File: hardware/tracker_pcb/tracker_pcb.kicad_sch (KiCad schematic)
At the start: 36 parts, among them IC1 DRV8244HQRYJRQ1, IC2 DRV8244HQRYJRQ1, IC3 THVD1426DRLR, J1 256-406, U1 TPS62933FDRLR, U2 ESP32C6_SEEED, X1 256-402

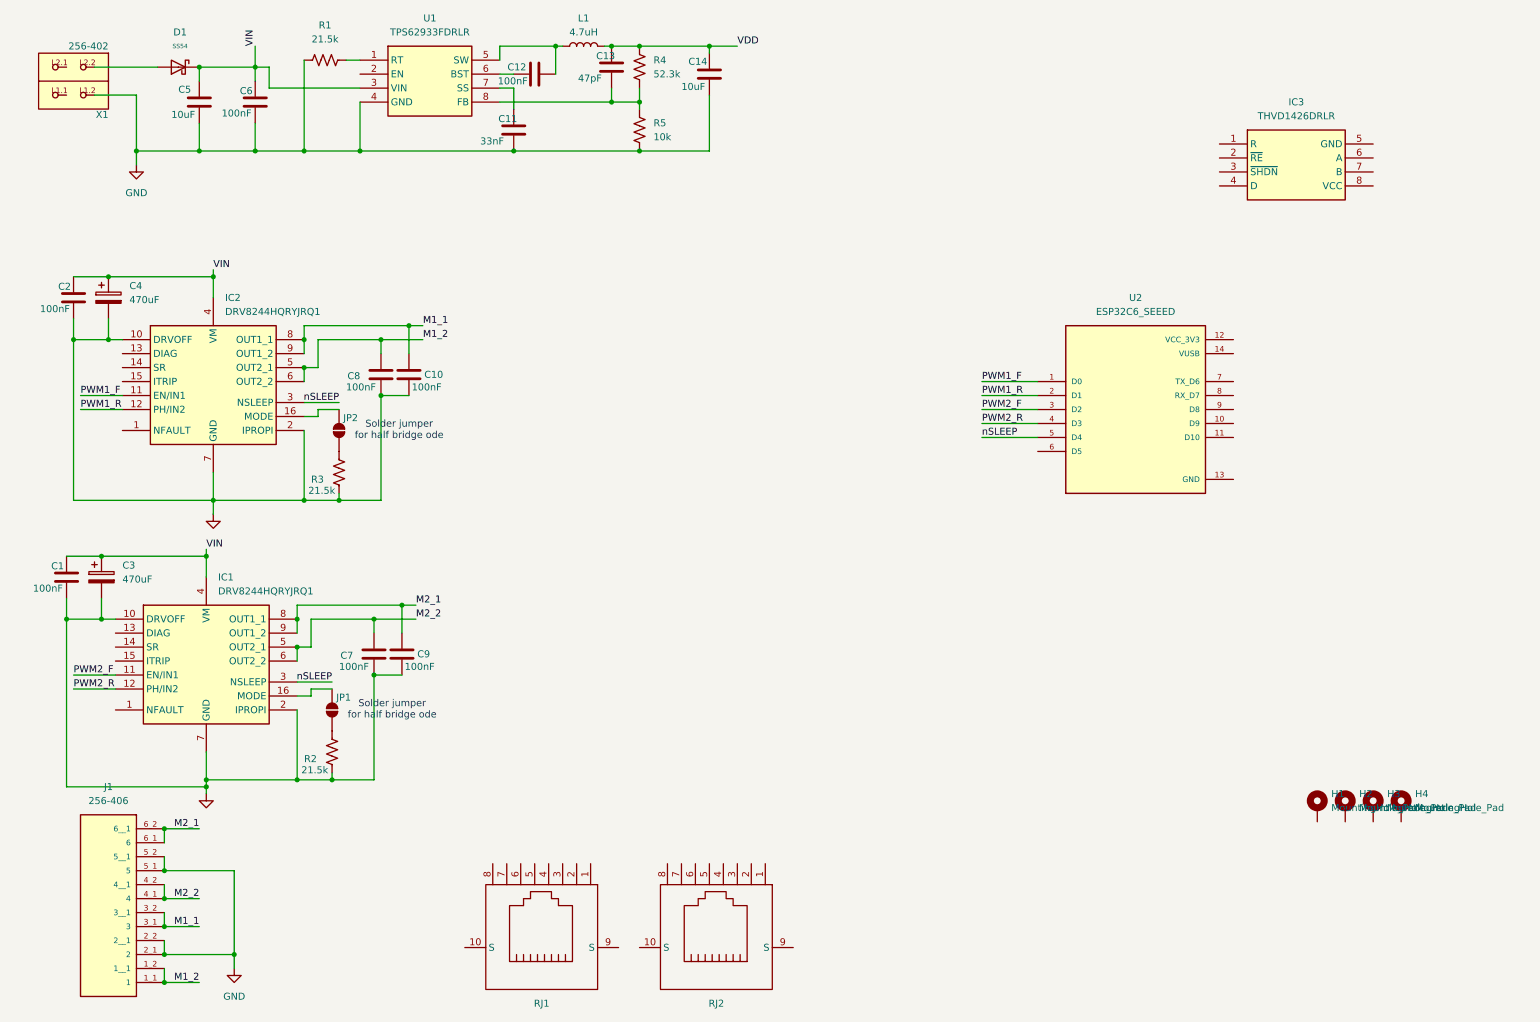
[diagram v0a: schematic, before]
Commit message: Hierarcical sheets
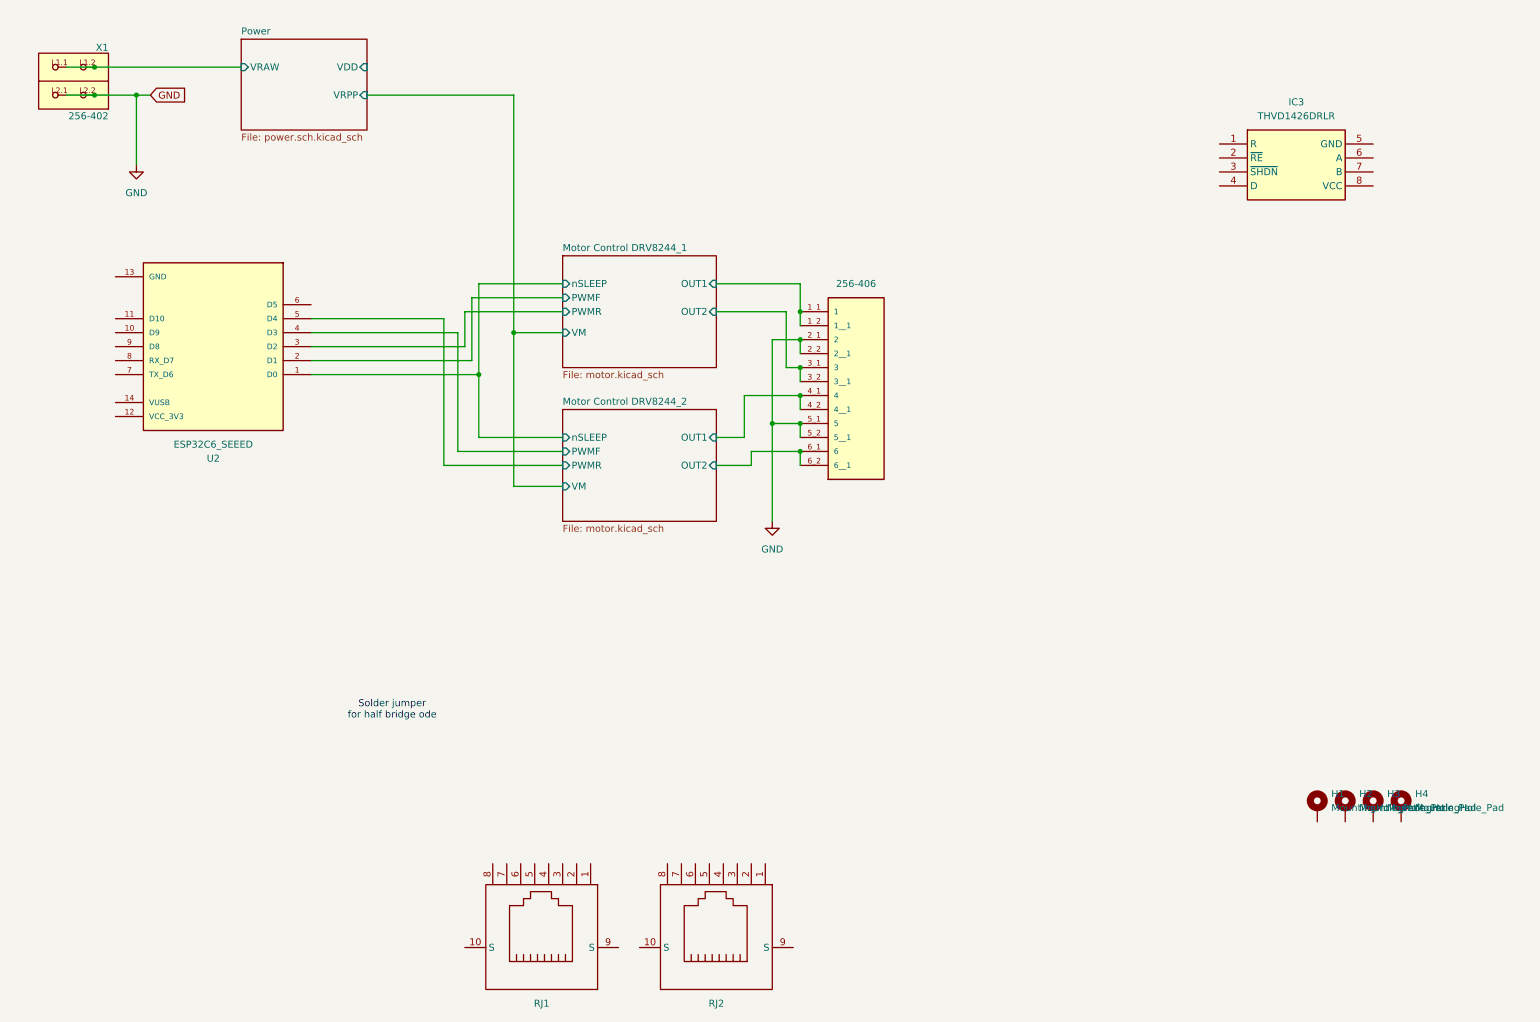
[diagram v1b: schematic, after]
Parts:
- removed C1, C10, C12, C2, C6, C7, C8, C9: 100nF, Capacitor_SMD:C_0603_1608Metric, symbol Device:C
- removed C11: 33nF, Capacitor_SMD:C_0603_1608Metric, symbol Device:C
- removed C13: 47pF, Capacitor_SMD:C_0603_1608Metric, symbol Device:C
- removed C14: 10uF, Capacitor_SMD:C_0603_1608Metric, symbol Device:C
- removed C3, C4: 470uF, Capacitor_SMD:CP_Elec_10x12.5, symbol Device:C_Polarized
- removed C5: 10uF, Capacitor_SMD:C_1206_3216Metric, symbol Device:C
- removed D1: SS54, Diode_SMD:D_SMA, symbol PCM_JLCPCB-Diodes:Schottky,SS54
- removed IC1, IC2: DRV8244HQRYJRQ1, footprint:DRV8244HQRYJRQ1, symbol symbol:DRV8244HQRYJRQ1
- removed JP1, JP2: SolderJumper_2_Open, Resistor_SMD:R_0402_1005Metric_Pad0.72x0.64mm_HandSolder, symbol Jumper:SolderJumper_2_Open
- removed L1: 4.7uH, Inductor_SMD:L_12x12mm_H6mm, symbol Device:L
- removed R1, R2, R3: 21.5k, Resistor_SMD:R_0603_1608Metric, symbol Device:R_US
- removed R4: 52.3k, Resistor_SMD:R_0603_1608Metric, symbol Device:R_US
- removed R5: 10k, Resistor_SMD:R_0603_1608Metric, symbol Device:R_US
- removed U1: TPS62933FDRLR, footprint:SOTFL50P160X60-8N, symbol symbol:TPS62933FDRLR
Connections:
- net GND: now also X1.L2.1, X1.L2.2; no longer X1.L1.2
- net Power/VRAW: now reaches X1.L1.1
- net Power/VRAW: now also X1.L1.2
- net M1_1 renamed Motor Control DRV8244_1/OUT2
- net M1_2 renamed Motor Control DRV8244_1/OUT1
- net M2_1 renamed Motor Control DRV8244_2/OUT2
- net M2_2 renamed Motor Control DRV8244_2/OUT1
- net PWM1_F renamed Motor Control DRV8244_1/nSLEEP
- net PWM1_R renamed Motor Control DRV8244_1/PWMF
- net PWM2_F renamed Motor Control DRV8244_1/PWMR
- net PWM2_R renamed Motor Control DRV8244_2/PWMF
- net nSLEEP renamed Motor Control DRV8244_2/PWMR
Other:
- added sheet Motor Control DRV8244_1 (motor.kicad_sch)
- added sheet Motor Control DRV8244_2 (motor.kicad_sch)
- added sheet Power (power.sch.kicad_sch)
- moved on the sheet: U2, X1

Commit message: More layout - adding rs485 an dinputmsheets
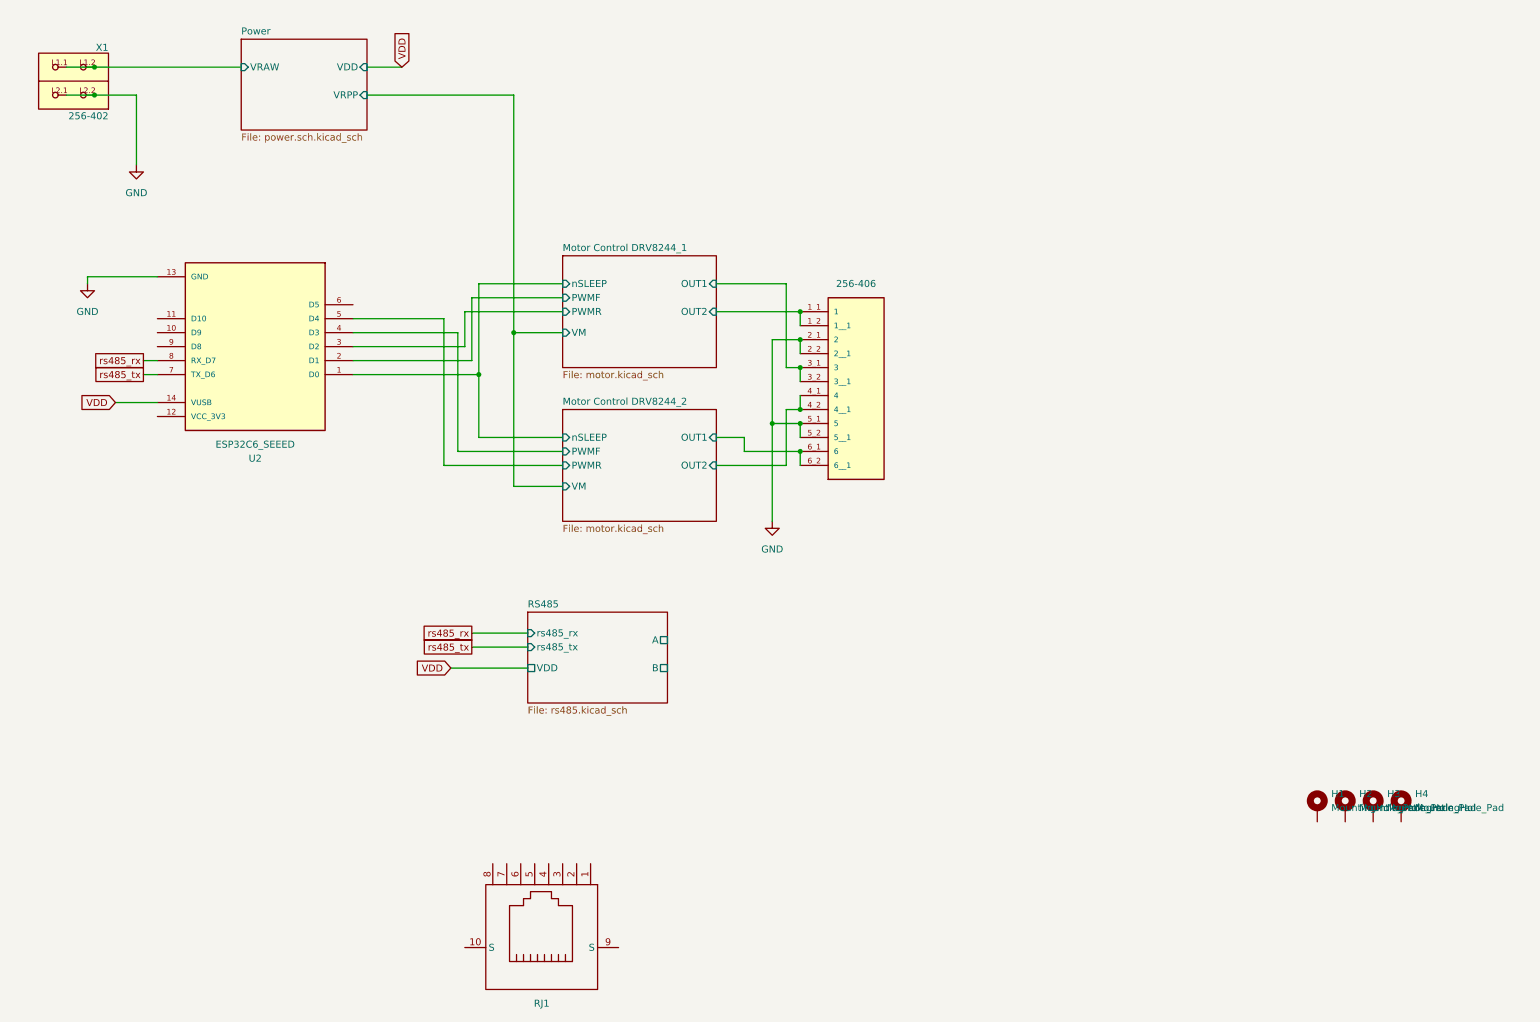
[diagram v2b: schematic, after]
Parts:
- removed IC3: THVD1426DRLR, footprint:SOTFL50P160X60-8N, symbol symbol:THVD1426DRLR
- removed RJ2: ~, footprint:RJ45-TH_R-RJ45R08P-B000, symbol symbol:R-RJ45R08P-B000
- RJ1: footprint footprint:RJ45-TH_R-RJ45R08P-B000 -> footprint:RJ45-TH_R-RJ45S08P-B000
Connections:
- net GND: now also U2.13 (GND)
- net Motor Control DRV8244_1/OUT1: now also J1.3_1 (3), J1.3_2 (3__1); no longer J1.1_1 (1), J1.1_2 (1__1)
- net Motor Control DRV8244_1/OUT2: now also J1.1_1 (1), J1.1_2 (1__1); no longer J1.3_1 (3), J1.3_2 (3__1)
- net Motor Control DRV8244_2/OUT1: now also J1.6_1 (6), J1.6_2 (6__1); no longer J1.4_1 (4), J1.4_2 (4__1)
- net Motor Control DRV8244_2/OUT2: now also J1.4_1 (4), J1.4_2 (4__1); no longer J1.6_1 (6), J1.6_2 (6__1)
- net VDD: now reaches U2.14 (VUSB)
- net rs485_tx: now reaches U2.7 (TX_D6)
- net rs485_rx: now reaches U2.8 (RX_D7)
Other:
- added sheet RS485 (rs485.kicad_sch)
- note removed: "Solder jumper for half bridge ode"
- moved on the sheet: U2

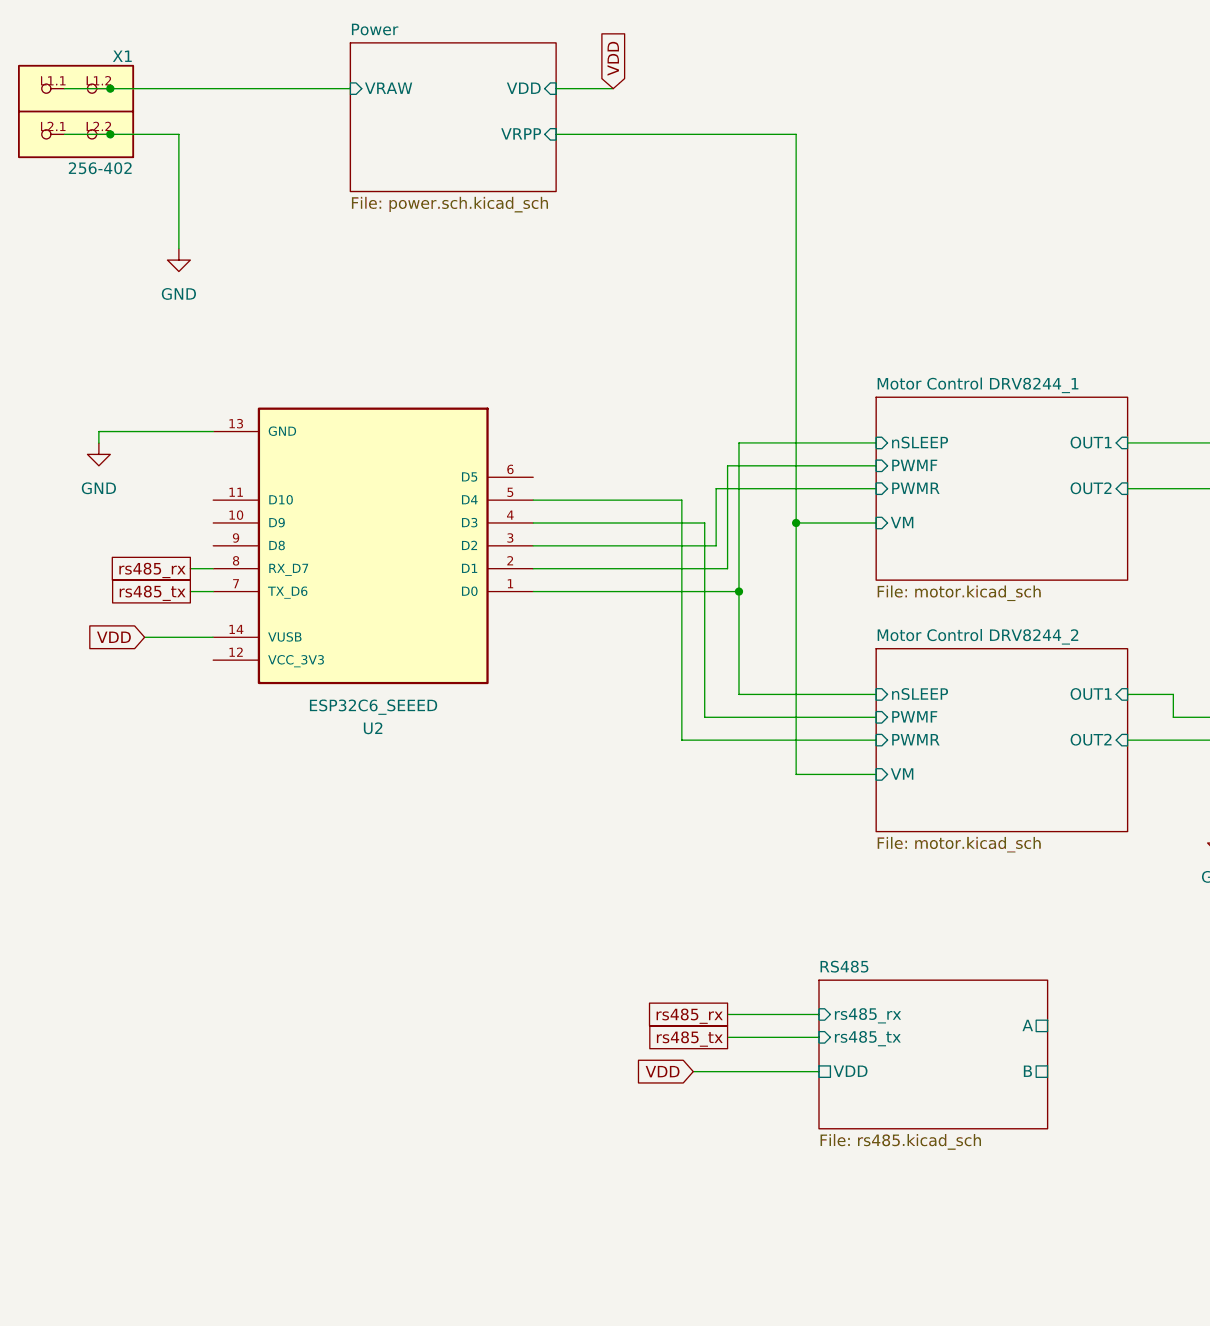
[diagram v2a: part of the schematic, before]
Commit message: add opto input module
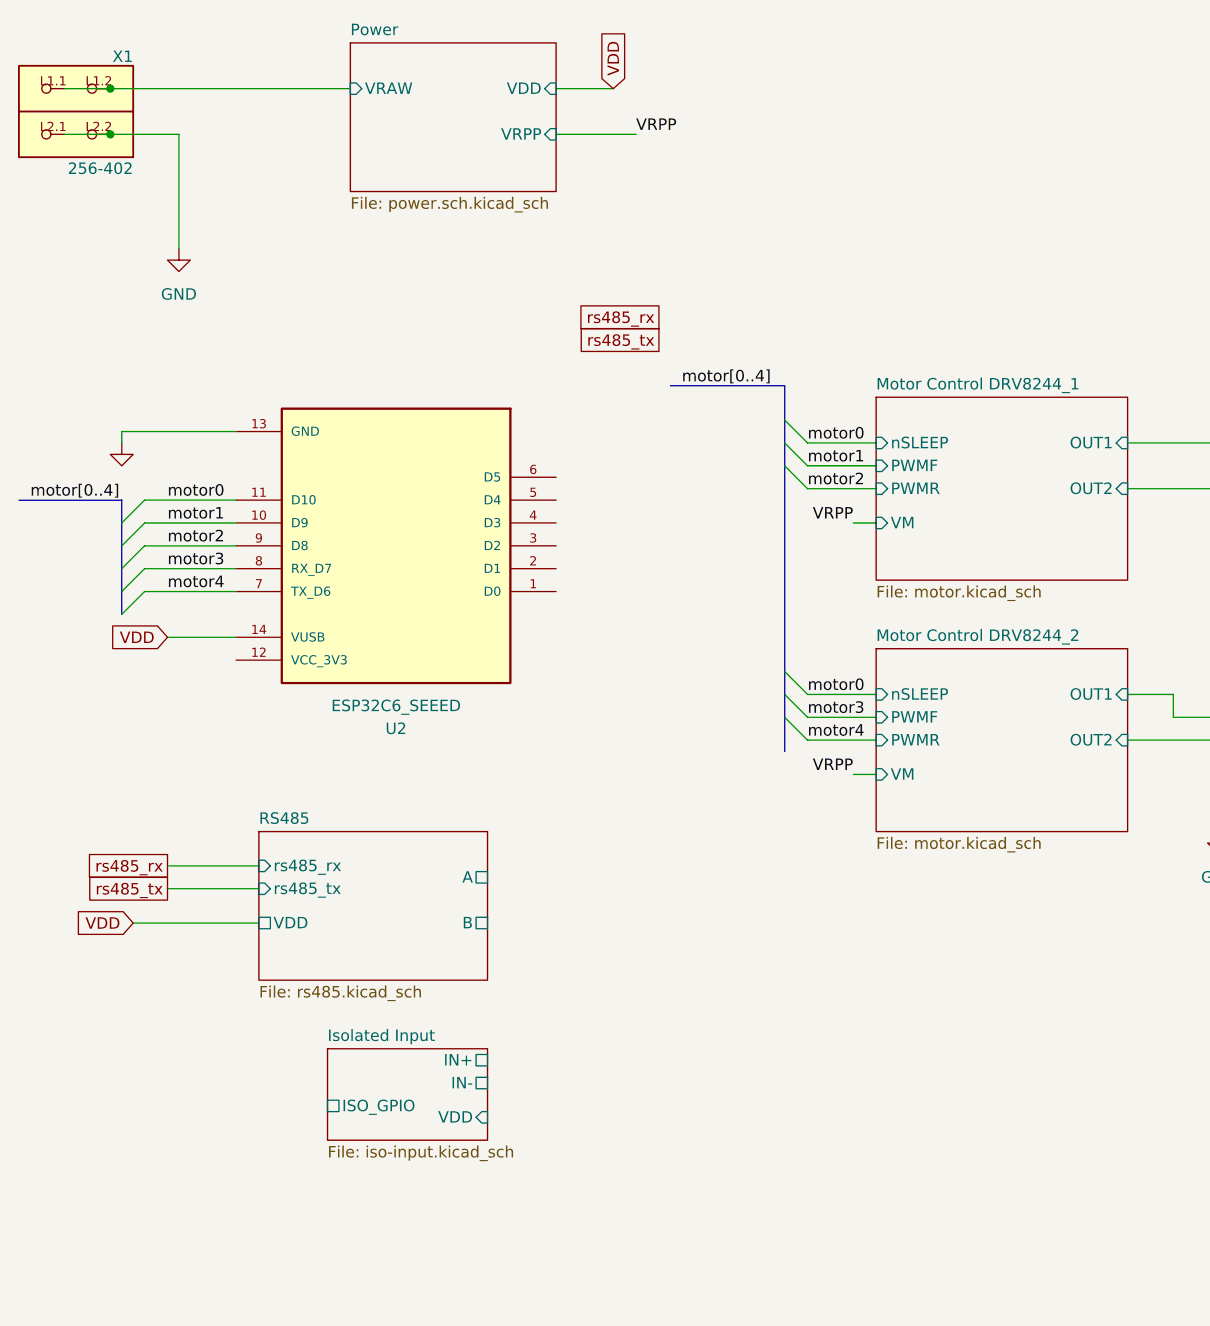
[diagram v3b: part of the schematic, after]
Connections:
- net rs485_rx: no longer U2.8 (RX_D7)
- net rs485_tx: no longer U2.7 (TX_D6)
- net motor1: now reaches U2.10 (D9)
- net motor0: now reaches U2.11 (D10)
- net motor2: now reaches U2.9 (D8)
- net Motor Control DRV8244_1/PWMF: no longer names the net of U2.2 (D1)
- net Motor Control DRV8244_1/PWMR: no longer names the net of U2.3 (D2)
- net Motor Control DRV8244_1/nSLEEP: no longer names the net of U2.1 (D0)
- net Motor Control DRV8244_2/PWMF: no longer names the net of U2.4 (D3)
- net Motor Control DRV8244_2/PWMR: no longer names the net of U2.5 (D4)
- new net motor3: U2.8 (RX_D7)
- new net motor4: U2.7 (TX_D6)
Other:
- added sheet Isolated Input (iso-input.kicad_sch)
- moved on the sheet: U2

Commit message: Work
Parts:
- added C9: 100nF, Capacitor_SMD:C_0603_1608Metric, symbol Device:C
- added J3: Screw_Terminal_01x03, Connector_PinHeader_2.54mm:PinHeader_1x03_P2.54mm_Vertical, symbol Connector:Screw_Terminal_01x03
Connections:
- net GND: now also RJ1.10 (S), RJ1.3, RJ1.6, RJ1.7, RJ1.8, RJ1.9 (S), C9.2, J3.1 (Pin_1)
- net Isolated Input/IN+: now also J3.2 (Pin_2)
- net RS485/A: now also RJ1.5
- net RS485/B: now also RJ1.4
- net VDD: now also RJ1.1, RJ1.2, C9.1
- net VRPP: now also J3.3 (Pin_3)
- net rs485_rx: now also U2.5 (D4)
- net rs485_tx: now also U2.6 (D5)
- net IN0: now reaches U2.1 (D0)
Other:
- sheet Isolated Input ports: added none; removed IN-
- note added: "BL"
- note added: "BL/WH"
- note added: "refer to T568B for pinout"
- moved on the sheet: RJ1

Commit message: WIP it so good
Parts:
- removed J3: Screw_Terminal_01x03, Connector_PinHeader_2.54mm:PinHeader_1x03_P2.54mm_Vertical, symbol Connector:Screw_Terminal_01x03
- added C11: 100nF, Capacitor_SMD:C_0603_1608Metric, symbol Device:C
- added J2: JL308-25409G01, TerminalBlock_TE-Connectivity:TerminalBlock_TE_282834-9_1x09_P2.54mm_Horizontal, symbol Connector:Screw_Terminal_01x09
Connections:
- net GND: now also C11.2, J2.3 (Pin_3), J2.6 (Pin_6), J2.9 (Pin_9)
- net Isolated Input/IN+: now also J2.2 (Pin_2)
- net VDD: now also C11.1
- net VRPP: now also J2.1 (Pin_1), J2.4 (Pin_4), J2.7 (Pin_7)
- net DIG1: now reaches U2.2 (D1)
- net DIG2: now reaches U2.3 (D2)
- net IN0 renamed DIG0
- new net Isolated Input1/IN+: J2.5 (Pin_5)
- new net Isolated Input2/IN+: J2.8 (Pin_8)
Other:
- added sheet Isolated Input1 (iso-input.kicad_sch)
- added sheet Isolated Input2 (iso-input.kicad_sch)
- moved on the sheet: U2
